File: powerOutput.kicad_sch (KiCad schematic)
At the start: 12 parts, among them J1 Screw_Terminal_01x08, J9 Screw_Terminal_01x08, K1 SANYOU_SRD-S-124D, K2 SANYOU_SRD-S-124D, K3 SANYOU_SRD-S-124D, K4 SANYOU_SRD-S-124D, U4 ULN2803CDW, U7 ULN2803CDW

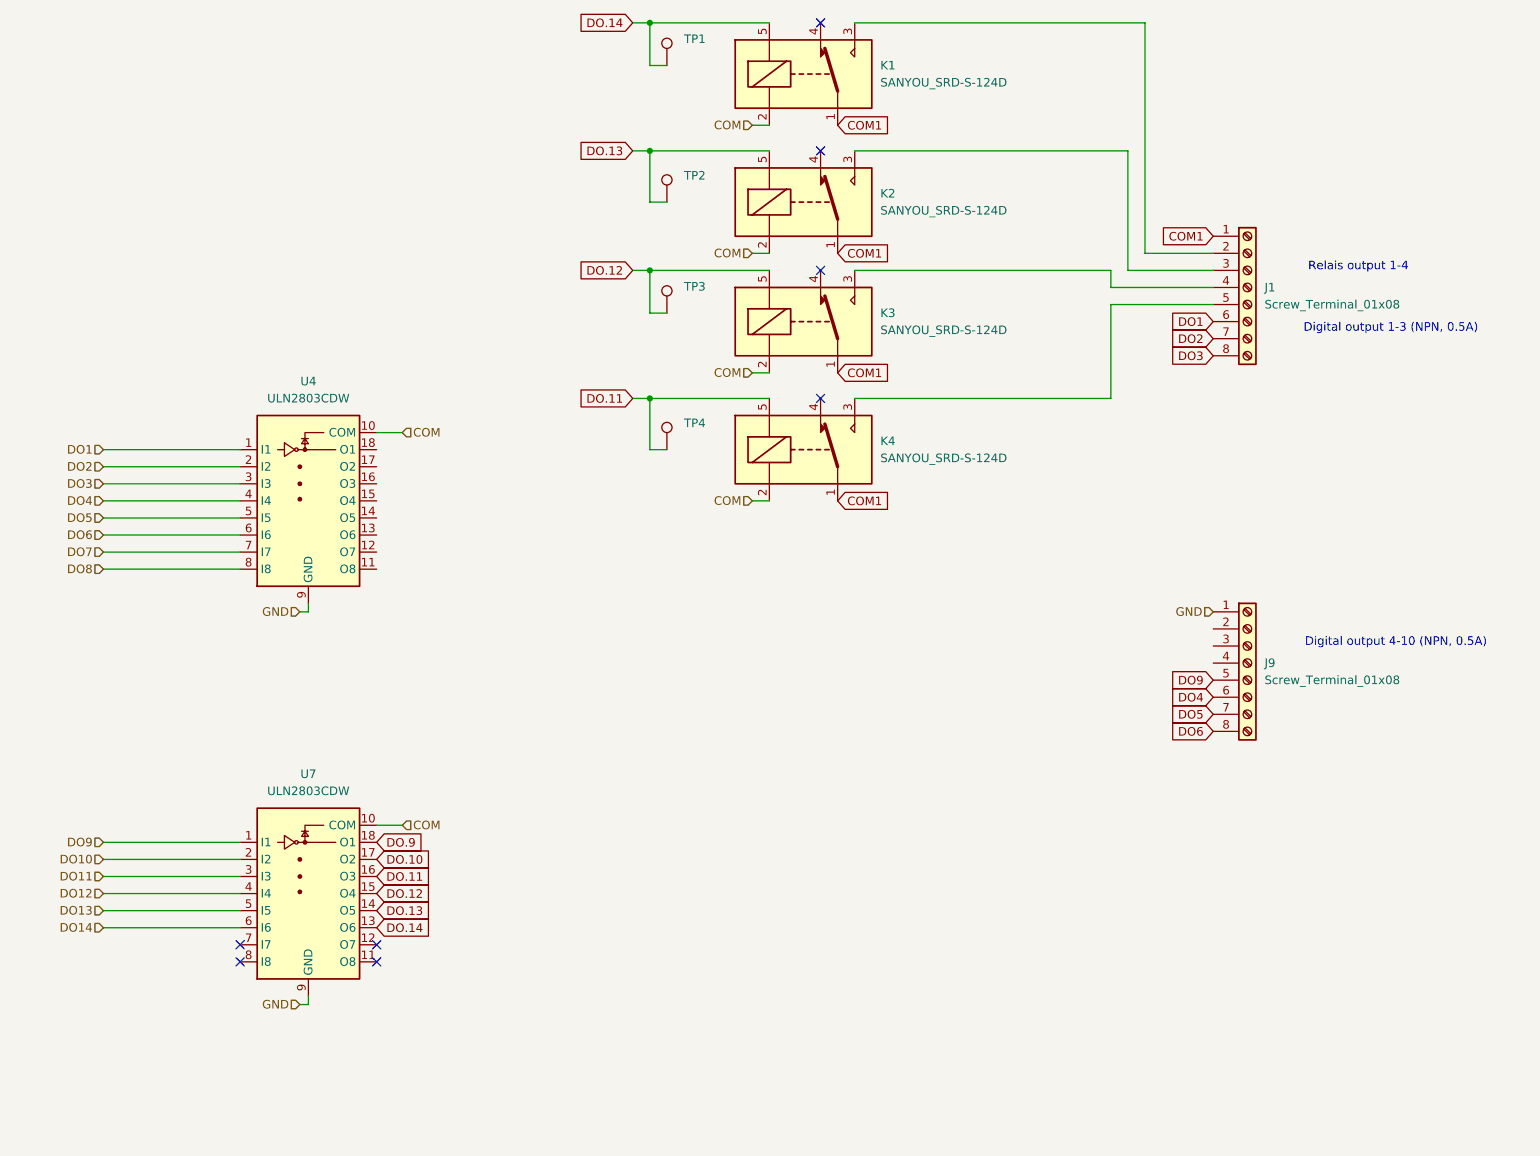
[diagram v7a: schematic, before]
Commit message: pcb layout finished
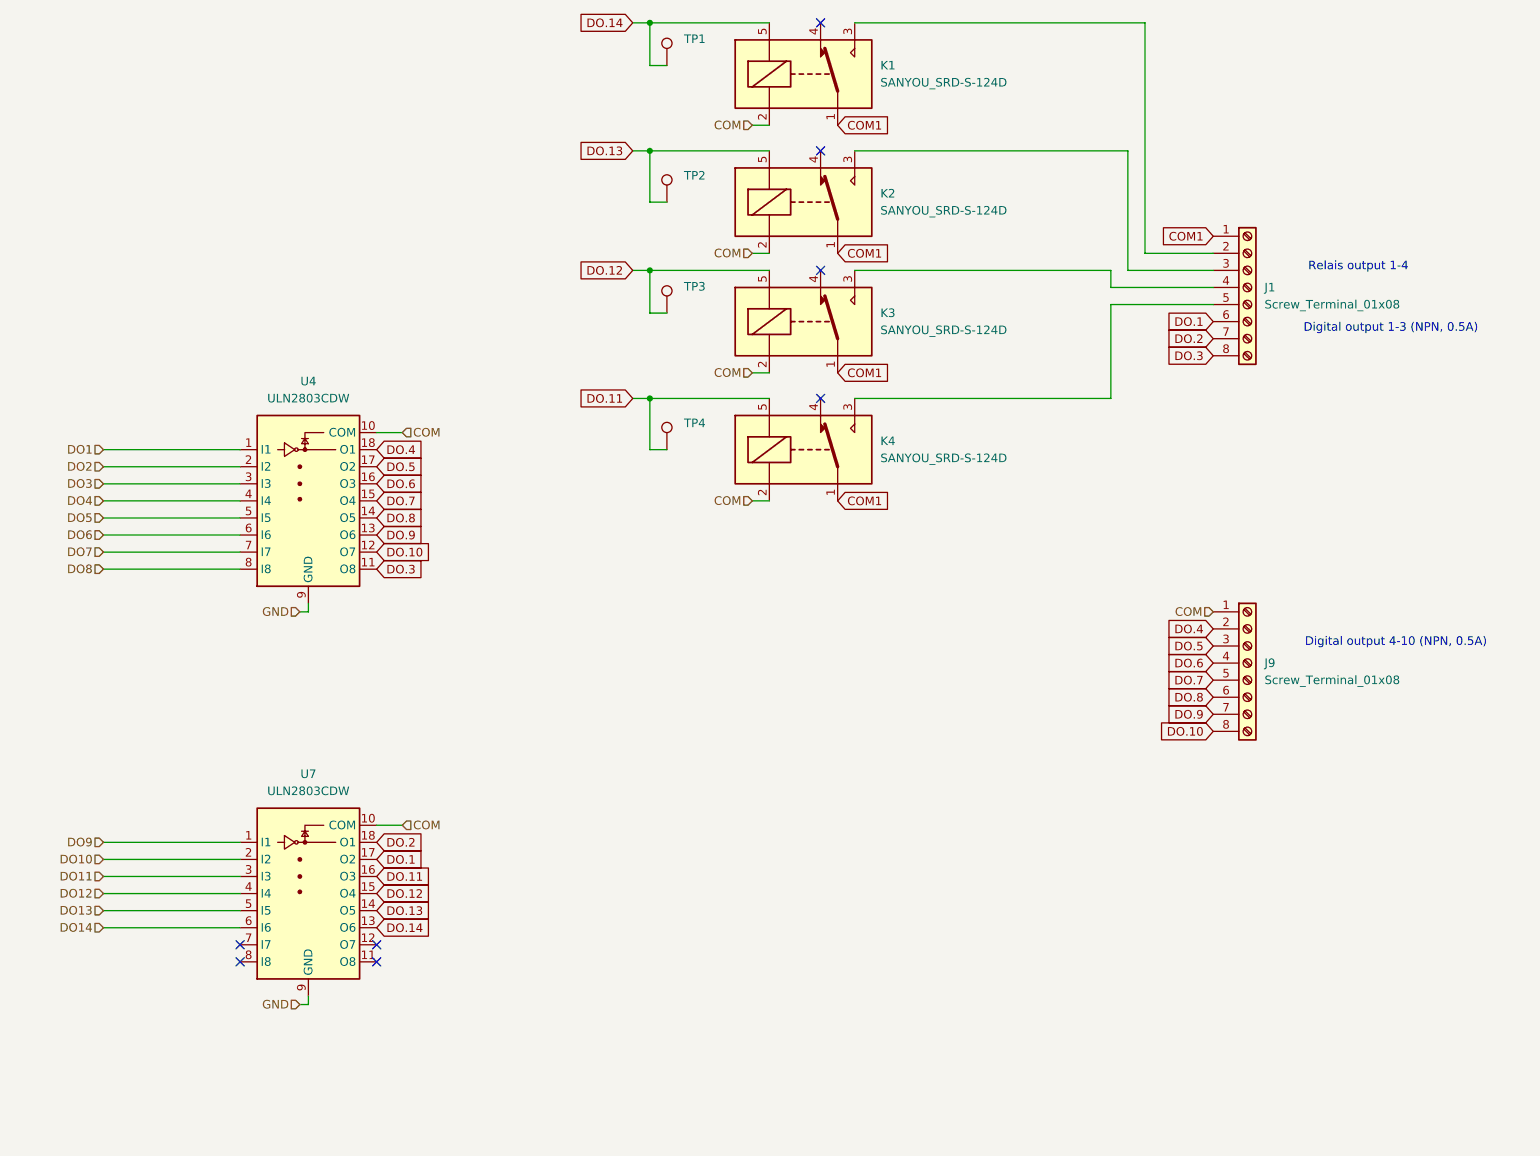
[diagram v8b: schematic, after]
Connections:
- net COM: now also J9.1 (Pin_1)
- net DO.10: now also J9.8 (Pin_8), U4.12 (O7); no longer U7.17 (O2)
- net DO.9: now also J9.7 (Pin_7), U4.13 (O6); no longer U7.18 (O1)
- net DO1: no longer J1.6 (Pin_6)
- net DO2: no longer J1.7 (Pin_7)
- net DO3: no longer J1.8 (Pin_8)
- net DO4: no longer J9.6 (Pin_6)
- net DO5: no longer J9.7 (Pin_7)
- net DO6: no longer J9.8 (Pin_8)
- net DO9: no longer J9.5 (Pin_5)
- net GND: no longer J9.1 (Pin_1)
- net DO.4: now reaches J9.2 (Pin_2)
- net DO.4: now also U4.18 (O1)
- net DO.5: now reaches J9.3 (Pin_3)
- net DO.5: now also U4.17 (O2)
- net DO.6: now reaches J9.4 (Pin_4)
- net DO.6: now also U4.16 (O3)
- net DO.3: now reaches U4.11 (O8)
- net DO.3: now also J1.8 (Pin_8)
- net DO.8: now reaches U4.14 (O5)
- net DO.8: now also J9.6 (Pin_6)
- net DO.7: now reaches U4.15 (O4)
- net DO.7: now also J9.5 (Pin_5)
- new net DO.1: J1.6 (Pin_6), U7.17 (O2)
- new net DO.2: J1.7 (Pin_7), U7.18 (O1)
